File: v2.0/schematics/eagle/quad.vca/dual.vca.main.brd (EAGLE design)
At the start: 75.2 x 39.4 mm, 61 parts, among them IC1 TL084P, IC2 LM13700N, Q1 2N3904, Q2 2N3906, Q3 2N3904, Q4 2N3906

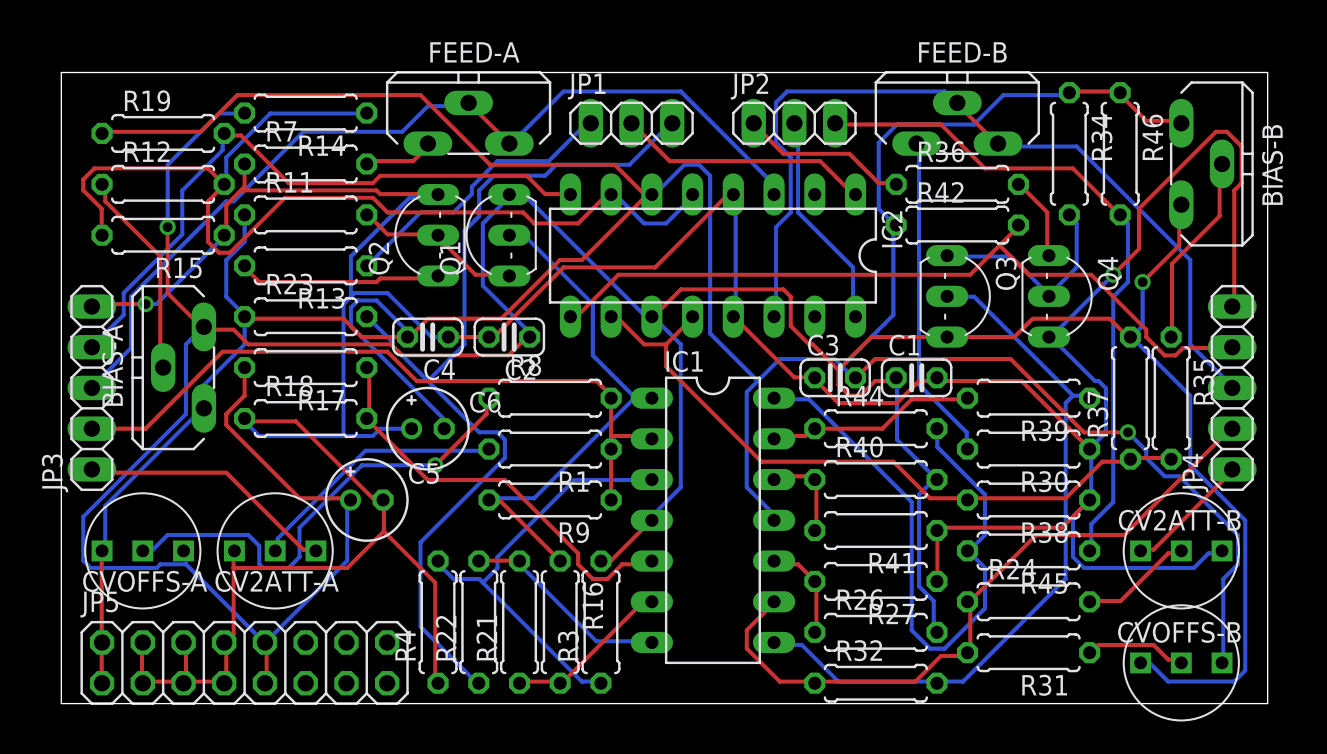
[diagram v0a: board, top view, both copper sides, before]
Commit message: Replaced trim pots with tested fixed values. Corrected error in PNP transisitor connection
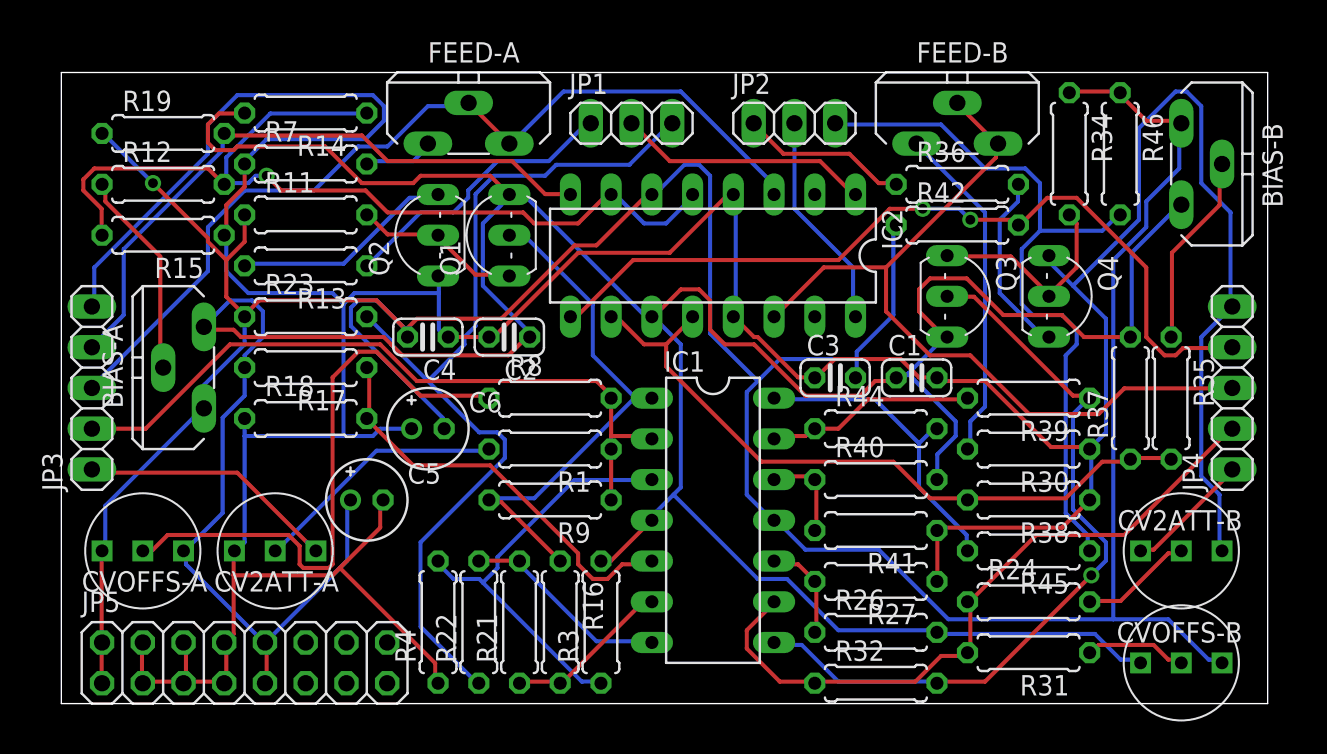
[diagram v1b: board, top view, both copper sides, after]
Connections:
- removed net N$30: Q4.1, R36.2
- removed net N$9: Q2.1, R13.2
- new net N$1: Q2.3, R13.2
- new net N$2: Q4.3, R36.2
- net 0V: now also Q2.1, Q4.1; no longer Q2.3, Q4.3
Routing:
- net 0V: track 242.9 -> 264.7 mm, vias 2 -> 0
- net N$41: track 38.8 -> 19.6 mm
- net -12V: track 226.8 -> 209.3 mm
- net N$1: track 0.00 -> 14.0 mm
- net +12V: track 239.5 -> 225.6 mm, vias 2 -> 0
- net N$9: track 12.7 -> 0.00 mm
- net N$2: track 0.00 -> 11.5 mm
- net N$5: track 29.5 -> 37.1 mm, vias 1 -> 0
- net N$15: track 64.2 -> 58.1 mm, vias 0 -> 1
- net N$30: track 5.24 -> 0.00 mm
- net N$43: track 42.3 -> 46.5 mm
- net OUT-B: track 48.2 -> 52.1 mm, vias 0 -> 2
- net IN-B: track 53.7 -> 50.1 mm
- net N$28: track 45.1 -> 47.9 mm, vias 0 -> 1
- net N$31: track 20.3 -> 21.3 mm
